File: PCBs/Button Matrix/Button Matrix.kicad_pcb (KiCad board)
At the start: 2 copper layers, 146.1 x 133.3 mm, 39 parts, among them J1 Conn_01x04_Pin, J2 Conn_01x04_Pin, SW1 SW_Push, SW10 SW_Push, SW11 SW_Push, SW12 SW_Push, SW13 SW_Push, SW14 SW_Push, SW15 SW_Push, SW16 SW_Push, SW2 SW_Push, SW3 SW_Push, SW4 SW_Push, SW5 SW_Push, SW6 SW_Push, SW7 SW_Push, SW8 SW_Push, SW9 SW_Push

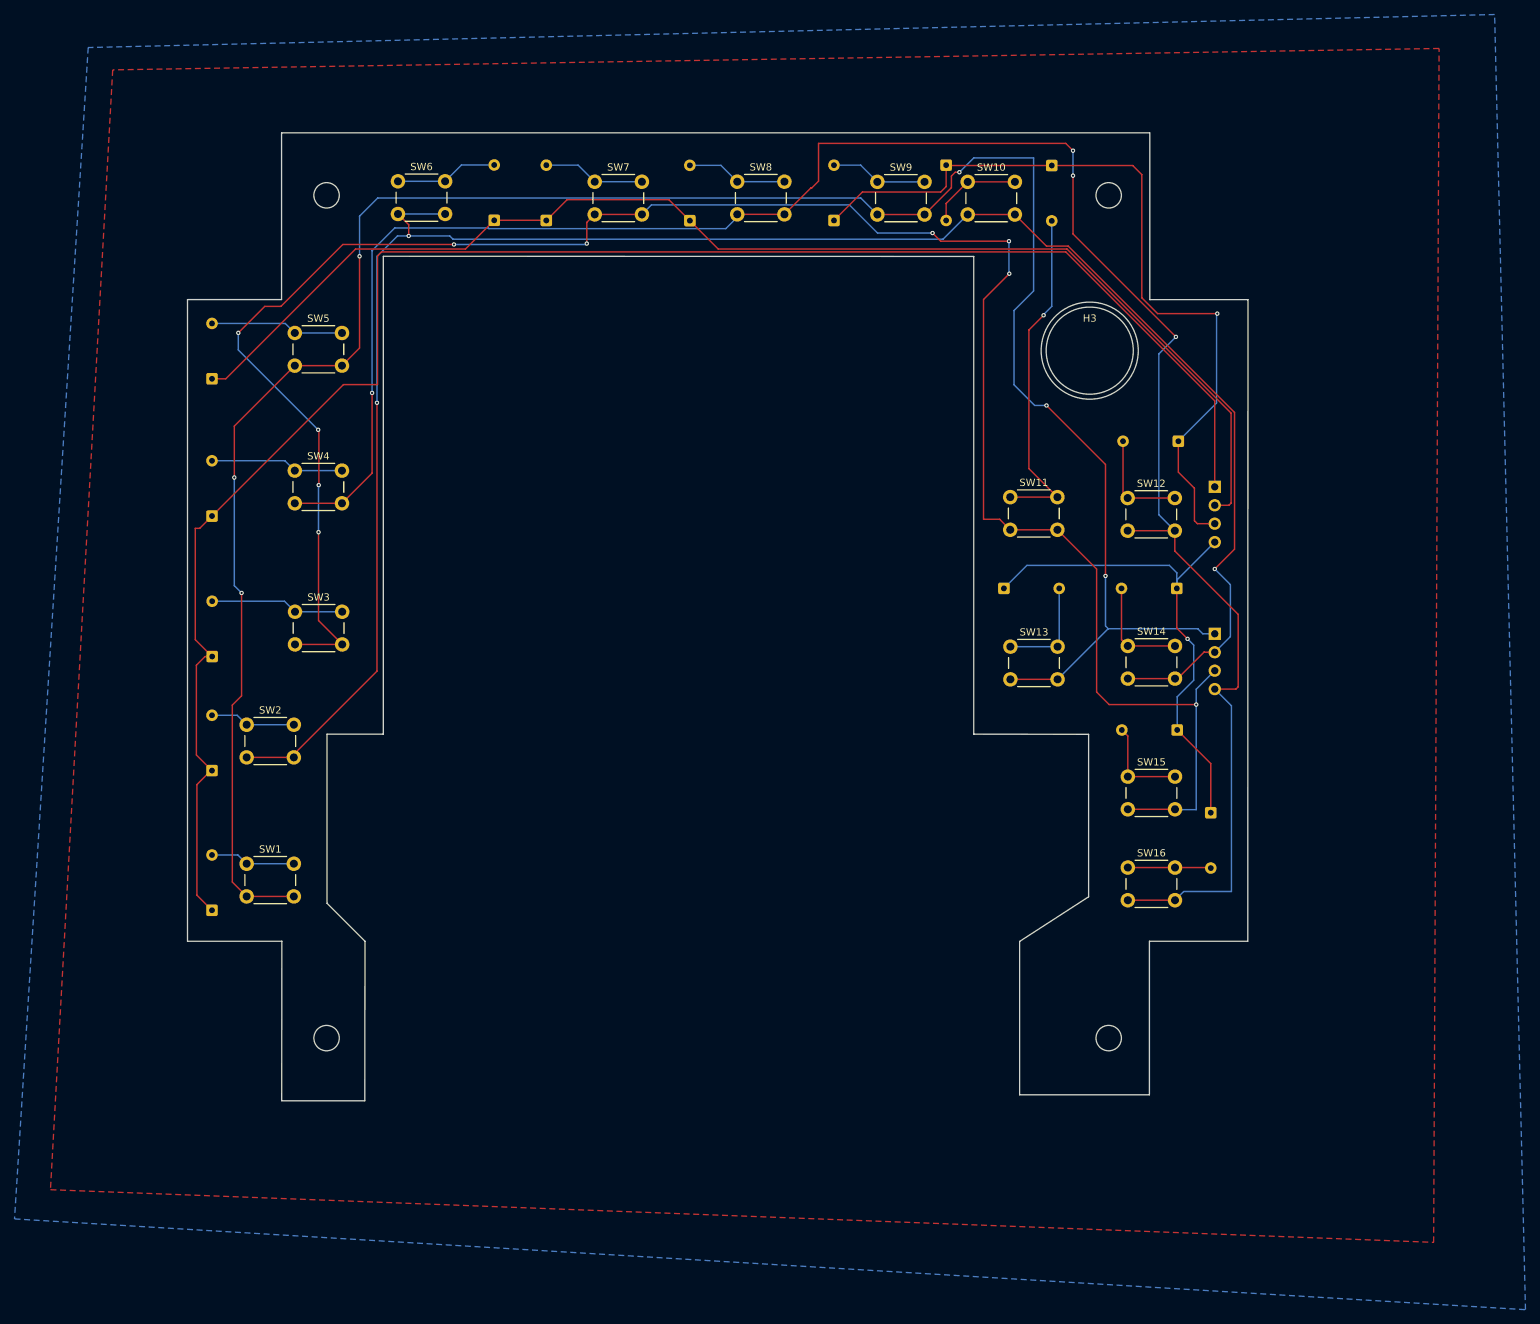
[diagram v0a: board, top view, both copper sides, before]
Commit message: Remove isolated copper fills from Button Matrix PCB and update clean DRC results
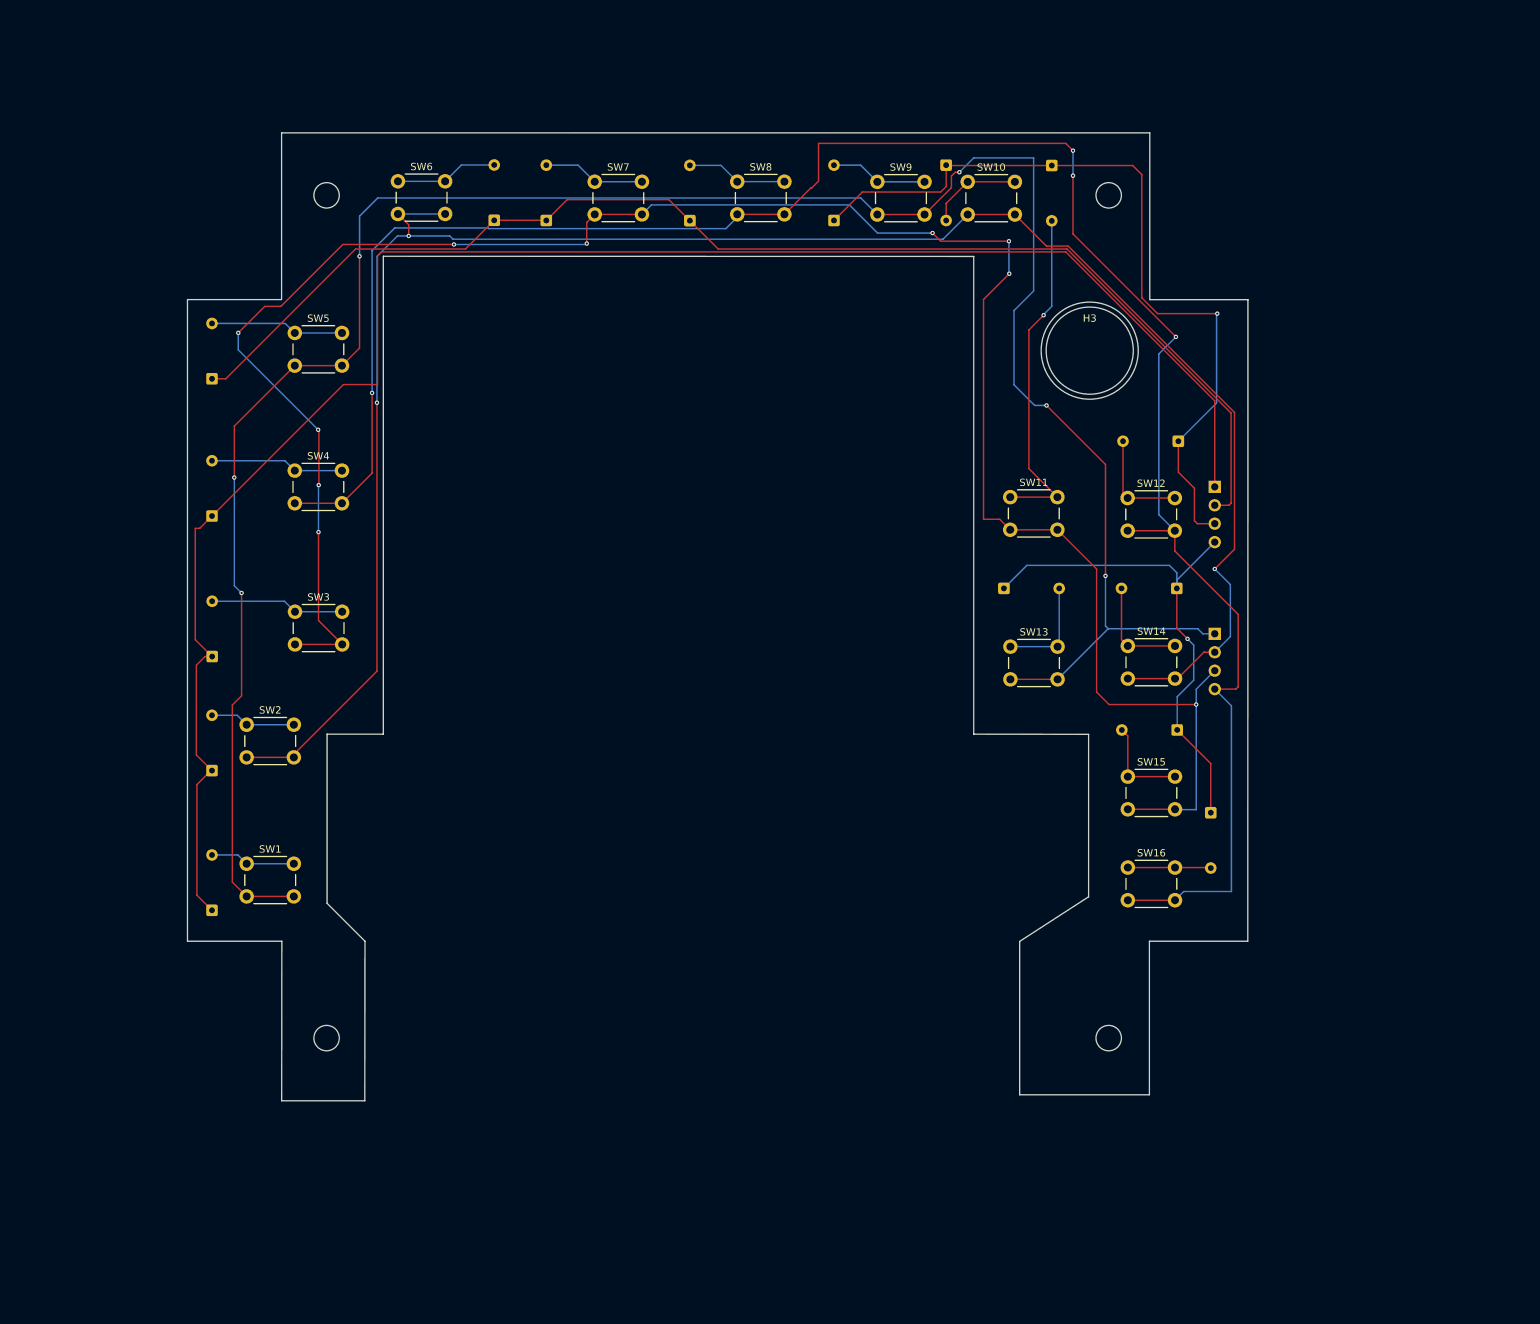
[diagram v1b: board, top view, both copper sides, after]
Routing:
- removed copper zone on B.Cu, net (none)
- removed copper zone on F.Cu, net (none)
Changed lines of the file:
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@@
 		(net "Net-(D10-K)")
-	)
-	(zone
-		(layer "F.Cu")
-		(hatch edge 0.5)
-		(connect_pads
-			(clearance 0.5)
-		)
-		(min_thickness 0.25)
-		(fill yes
-			(thermal_gap 0.5)
-			(thermal_bridge_width 0.5)
-			(island_removal_mode 1)
-		)
-		(polygon
-			(pts
-				(xy 40.55 30.45) (xy 31.975 184.7) (xy 222.5 191.95) (xy 223.25 27.5)
-			)
-		)
-	)
-	(zone
-		(layer "B.Cu")
-		(hatch edge 0.5)
-		(priority 1)
-		(connect_pads
-			(clearance 0.5)
-		)
-		(min_thickness 0.25)
-		(fill yes
-			(thermal_gap 0.5)
-			(thermal_bridge_width 0.5)
-			(island_removal_mode 1)
-		)
-		(polygon
-			(pts
-				(xy 37.175 27.375) (xy 27.025 188.725) (xy 235.15 201.225) (xy 230.9 22.825)
-			)
-		)
 	)
 	(group "ARC-210 faceplate - PC Flights DXF - 1:1"

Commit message: Release final Button Matrix PCB v3.1 with regenerated Gerbers, drills and fit-confirmed documentation
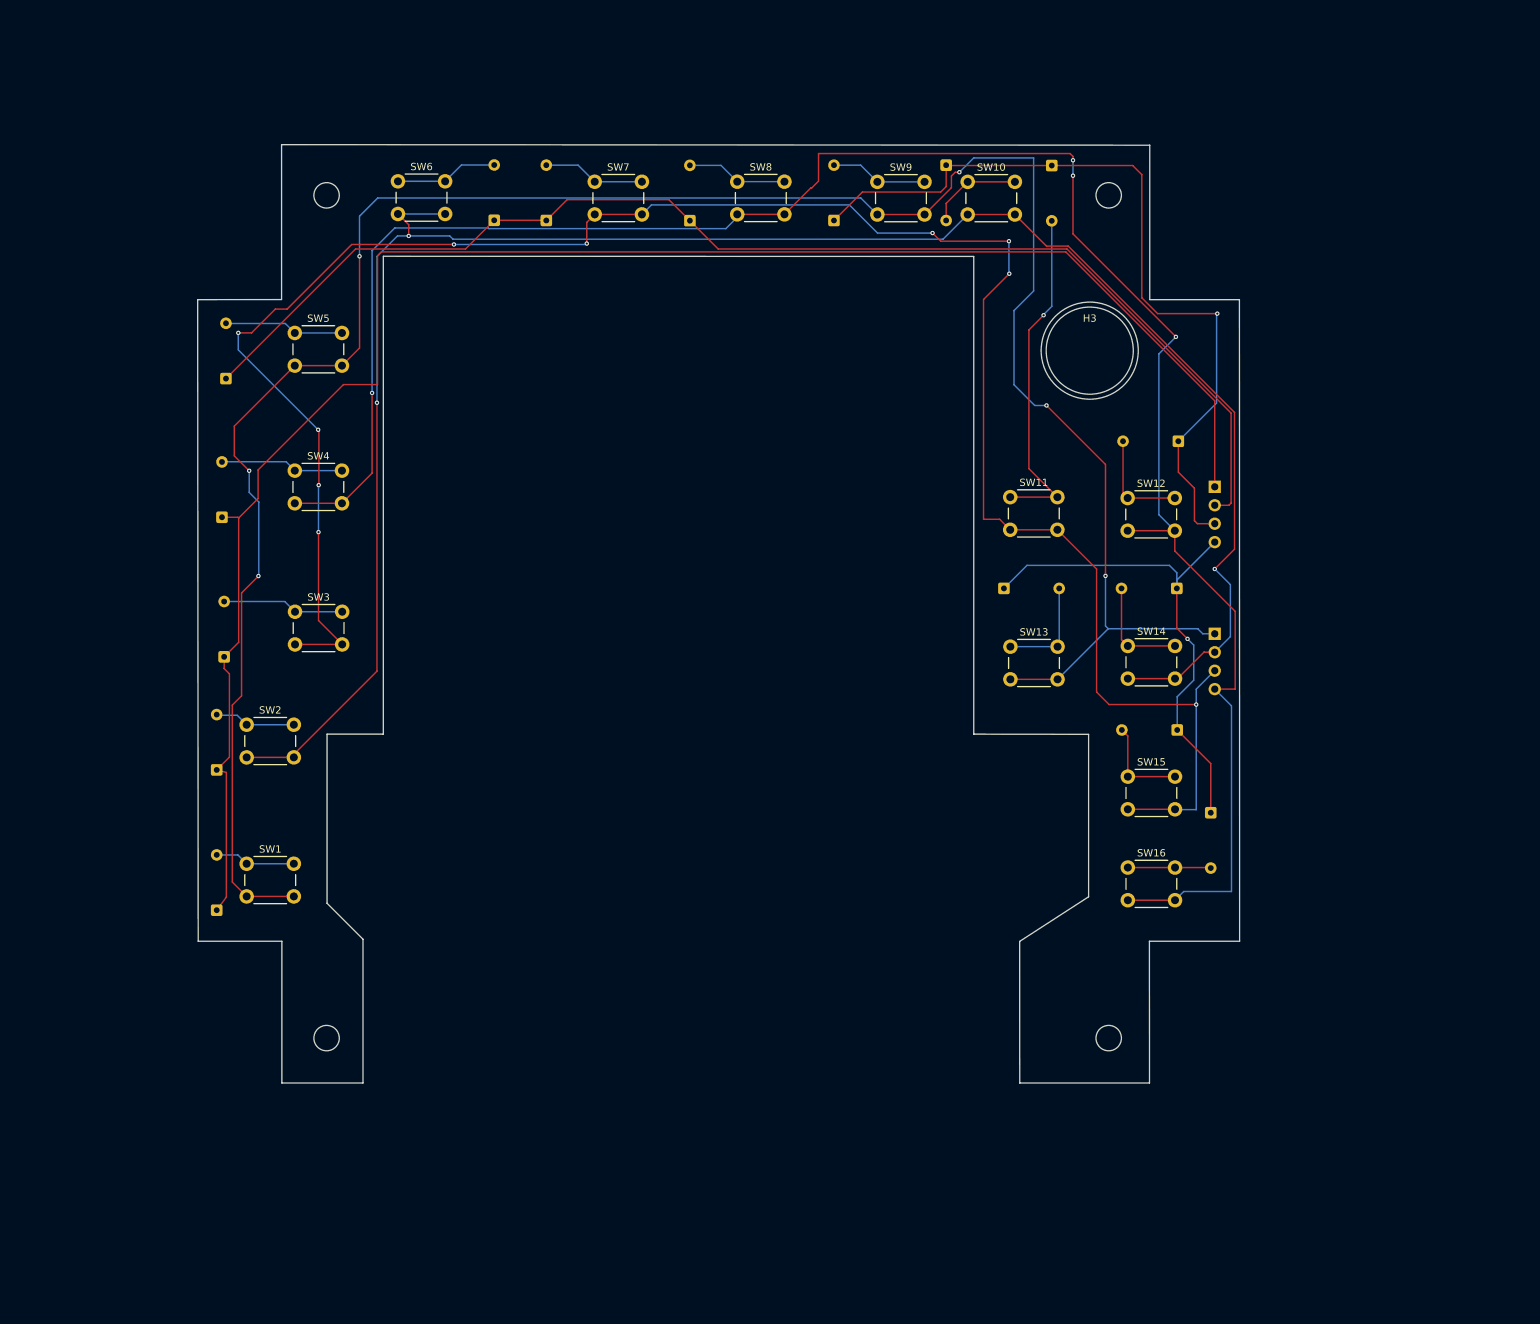
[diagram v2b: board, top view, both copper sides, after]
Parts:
- moved D9 1.93 mm to (56.1, 73.0)
- moved D7 1.65 mm to (55.9, 111.3)
- moved D8 1.38 mm to (55.6, 92.1)
- moved D6 0.66 mm to (54.9, 126.9)
- moved D5 0.65 mm to (54.9, 146.2)
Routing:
- net Net-(D5-K): track 244.7 -> 221.6 mm
- net Net-(D8-A): track 18.5 -> 6.50 mm
- net Net-(J2-Pin_4): track 288.2 -> 285.3 mm
- net Net-(J2-Pin_1): track 315.5 -> 317.4 mm
- net Net-(D9-A): track 18.4 -> 16.5 mm
- net Net-(D10-K): track 177.6 -> 175.7 mm
- net Net-(D7-A): track 18.5 -> 16.8 mm
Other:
- board size 146.1 x 133.3 mm -> 143.5 x 129.2 mm
- board text added: "ARC-210 v3.1"
- board text removed: "ARC-210 v3.0"
